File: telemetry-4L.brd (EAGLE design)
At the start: 69.8 x 22.9 mm, 69 parts, among them SW1 MF-SW-TACT-4.2MM, SW2 PCM12SMTR, U1 ATSAMD21G18A-MUT, U2 SPX3819M5-L-3-0, U3 MCP73831T-2ACI/OT, U4 IRLML6344TRPBF, U5 SIM868, U6 BMP280, U7 MPU-9250, U8 TPS61253YFFR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

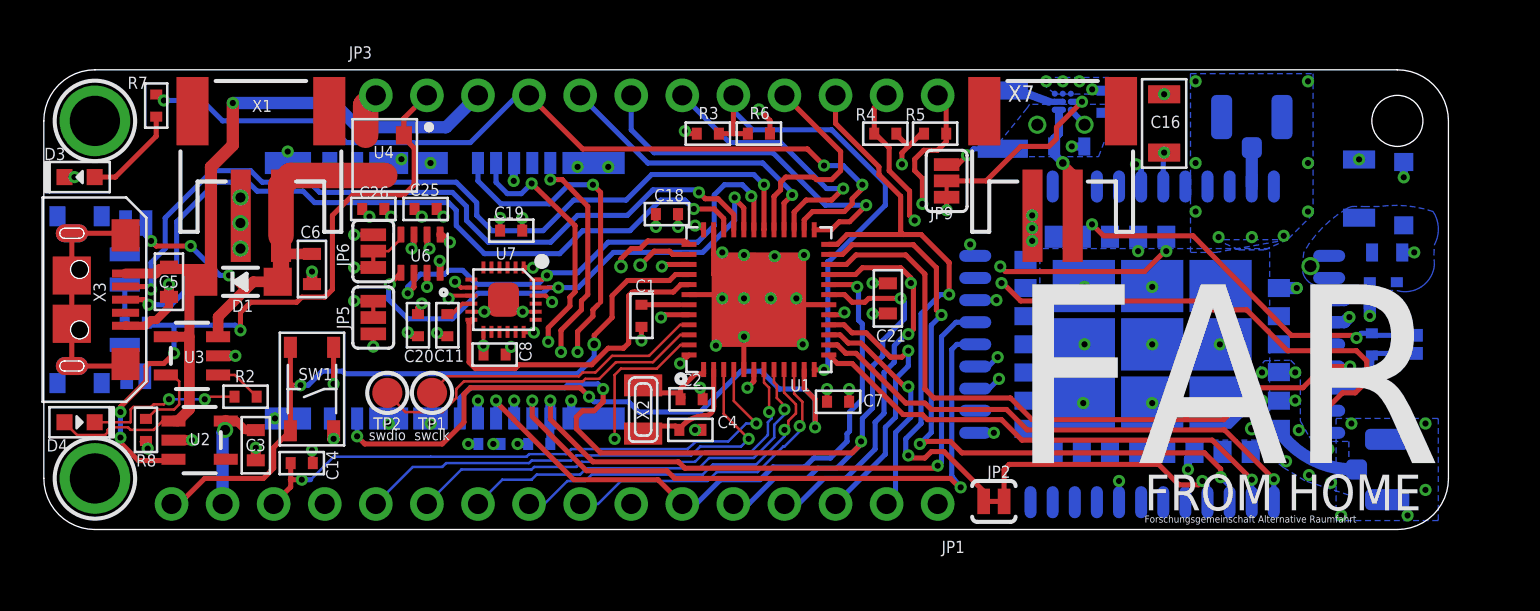
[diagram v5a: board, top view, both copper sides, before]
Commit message: Added MPR and POPULATE attributes - didnt seem to do anything though
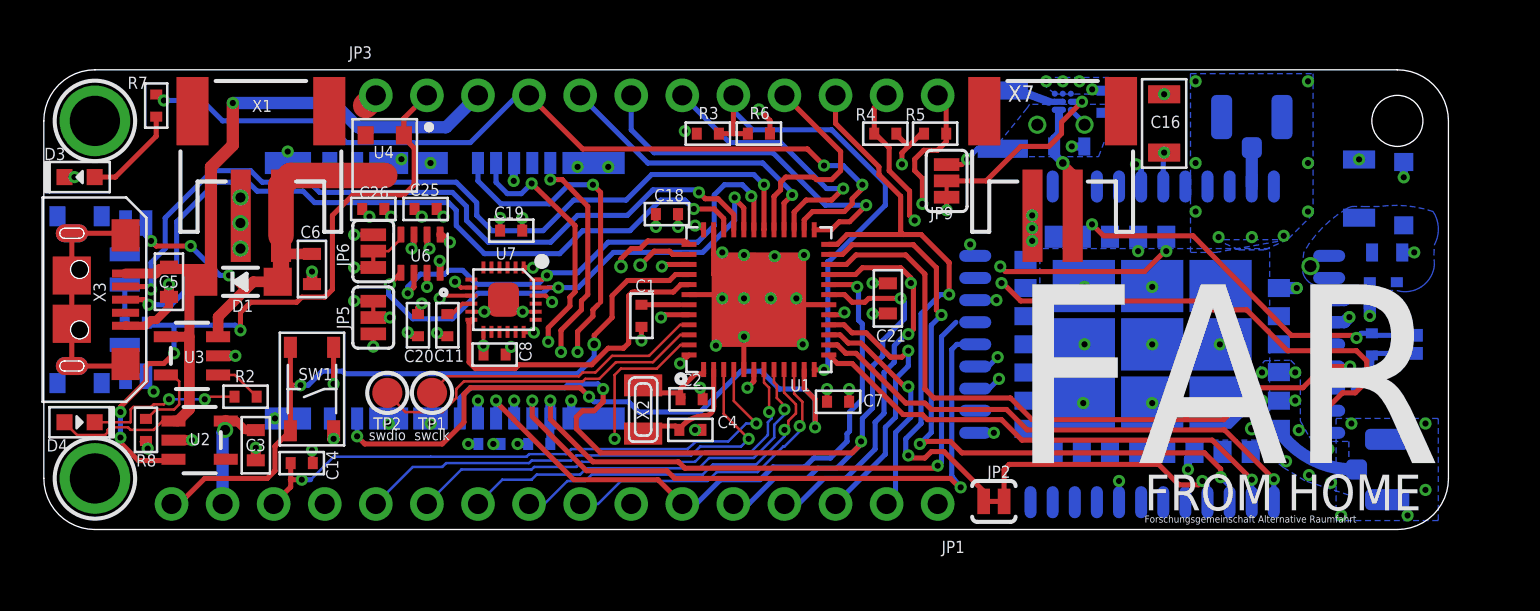
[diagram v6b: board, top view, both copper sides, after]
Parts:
- JP7: value JUMPER-PAD-2-NOYES_SILK -> JUMPER-PAD-2-NC_BY_TRACE; device SparkFun-Passives:PAD-JUMPER-2-NO_YES_SILK -> SparkFun-Passives:PAD-JUMPER-2-NC_BY_TRACE_YES_SILK
- L1: value 1277AS-H-1R0M=P2 -> 1uH
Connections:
- new net P$1: JP3.1
- net VBAT_ON: no longer JP3.1
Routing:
- net VBAT_ON: track 59.2 -> 53.1 mm
- net N$2: track 1.19 -> 5.59 mm, vias 1 -> 2
- net GND: track 70.4 -> 71.7 mm, vias 114 -> 115
- net VDD_EXT_2V8: track 5.17 -> 3.98 mm
- net SIM_VDD: track 31.9 -> 31.0 mm
- net P$1: track 0.00 -> 0.71 mm

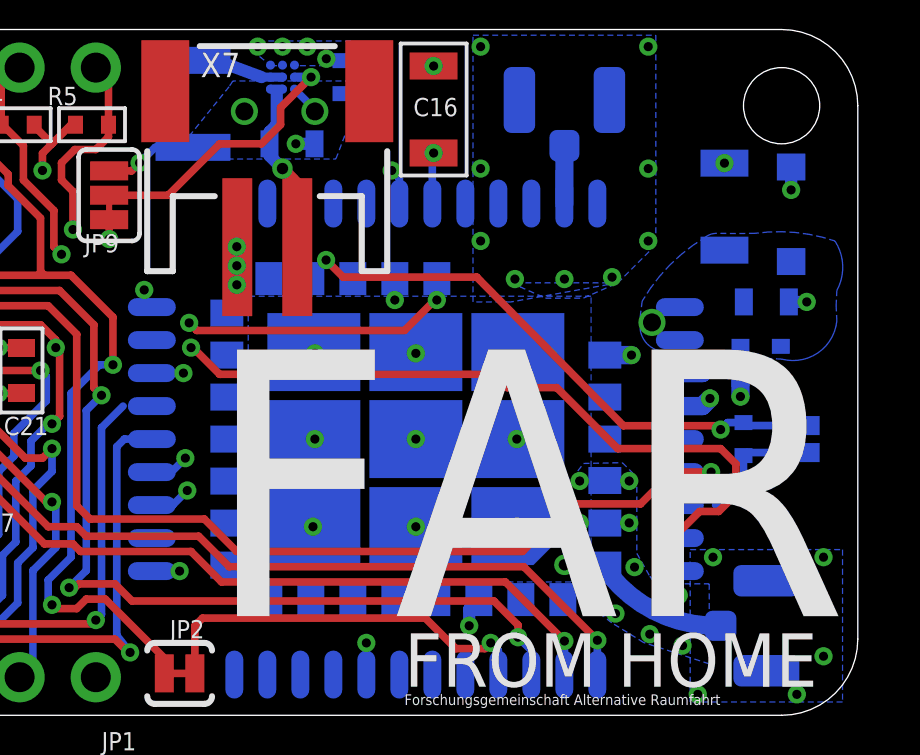
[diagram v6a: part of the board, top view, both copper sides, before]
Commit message: Added a 100uF cap to 5V output
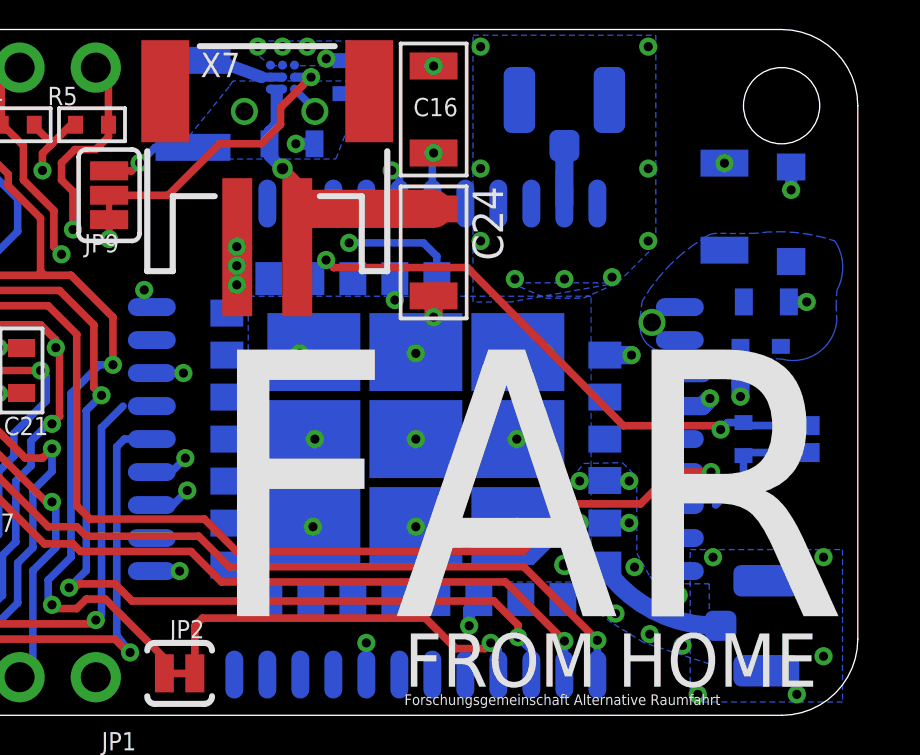
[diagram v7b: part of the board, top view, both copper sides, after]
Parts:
- added C24: 100uF, MF_Passives:C1206
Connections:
- net 5.0V: now also C24.P$1
- net GND: now also C24.P$2
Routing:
- net TX5/GPS_RX: track 34.9 -> 40.4 mm, vias 3 -> 2
- net 5.0V: track 6.26 -> 11.7 mm
- net STATUS: track 45.3 -> 41.7 mm, vias 3 -> 2
- net RX5/GPS_TX: track 31.2 -> 30.3 mm
- net GND: track 71.7 -> 72.4 mm, vias 115 -> 116

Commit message: tweaks
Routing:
- net TX5/GPS_RX: track 40.4 -> 39.9 mm
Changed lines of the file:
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@@
 <wire x1="40.1955" y1="13.462" x2="45.0215" y2="13.462" width="0.254" layer="15"/>
 <wire x1="45.0215" y1="13.462" x2="45.6565" y2="12.827" width="0.254" layer="15"/>
-<wire x1="54.483" y1="12.827" x2="45.6565" y2="12.827" width="0.254" layer="15"/>
-<wire x1="54.737" y1="14.605" x2="54.0385" y2="14.605" width="0.254" layer="15"/>
+<wire x1="54.229" y1="12.827" x2="45.6565" y2="12.827" width="0.254" layer="15"/>
+<wire x1="54.483" y1="14.605" x2="54.0385" y2="14.605" width="0.254" layer="15"/>
 <wire x1="54.0385" y1="14.605" x2="52.8955" y2="15.748" width="0.254" layer="15"/>
 <via x="52.8955" y="15.748" extent="1-16" drill="0.3048"/>
@@
 <wire x1="55.8165" y1="15.3035" x2="55.8165" y2="14.559" width="0.254" layer="16"/>
 <wire x1="55.8165" y1="14.559" x2="55.818" y2="14.5575" width="0.254" layer="16"/>
-<wire x1="54.483" y1="12.827" x2="55.1815" y2="13.5255" width="0.254" layer="15"/>
-<wire x1="55.1815" y1="13.5255" x2="55.1815" y2="14.1605" width="0.254" layer="15"/>
-<wire x1="55.1815" y1="14.1605" x2="54.737" y2="14.605" width="0.254" layer="15"/>
+<wire x1="54.229" y1="12.827" x2="54.9275" y2="13.5255" width="0.254" layer="15"/>
+<wire x1="54.9275" y1="13.5255" x2="54.9275" y2="14.1605" width="0.254" layer="15"/>
+<wire x1="54.9275" y1="14.1605" x2="54.483" y2="14.605" width="0.254" layer="15"/>
 </signal>
 <signal name="RX5/GPS_TX">
 <contactref element="U1" pad="38"/>
 <contactref element="U5" pad="61_"/>
-<wire x1="54.418" y1="14.5575" x2="54.418" y2="13.843" width="0.254" layer="16"/>
-<via x="54.418" y="13.843" extent="1-16" drill="0.3048"/>
+<wire x1="54.418" y1="14.5575" x2="54.164" y2="13.843" width="0.254" layer="16"/>
+<via x="54.164" y="13.843" extent="1-16" drill="0.3048"/>
 <wire x1="32.085" y1="13.68" x2="31.278" y2="13.68" width="0.254" layer="1"/>
 <wire x1="31.278" y1="13.68" x2="31.115" y2="13.843" width="0.254" layer="1"/>
@@
 <wire x1="45.974" y1="13.335" x2="46.6725" y2="13.335" width="0.254" layer="15"/>
 <wire x1="46.6725" y1="13.335" x2="47.0535" y2="13.716" width="0.254" layer="15"/>
-<wire x1="54.291" y1="13.97" x2="54.418" y2="13.843" width="0.254" layer="15"/>
-<wire x1="47.0535" y1="13.716" x2="54.2925" y2="13.716" width="0.254" layer="15"/>
-<wire x1="54.2925" y1="13.716" x2="54.4195" y2="13.843" width="0.254" layer="15"/>
-<wire x1="54.4195" y1="13.843" x2="54.418" y2="13.843" width="0.254" layer="15"/>
+<wire x1="53.021" y1="13.97" x2="54.164" y2="13.843" width="0" layer="19" extent="1-16"/>
+<wire x1="47.0535" y1="13.716" x2="54.0385" y2="13.716" width="0.254" layer="15"/>
+<wire x1="54.0385" y1="13.716" x2="54.1655" y2="13.843" width="0.254" layer="15"/>
+<wire x1="54.1655" y1="13.843" x2="54.164" y2="13.843" width="0.254" layer="15"/>
 </signal>
 <signal name="GPS_EN_">
@@
 <contactref element="SW2" pad="O"/>
 <contactref element="JP7" pad="2"/>
-<wire x1="4.028" y1="9.18" x2="4.122" y2="9.086" width="0.254" layer="16"/>
-<wire x1="4.122" y1="9.086" x2="4.064" y2="7.62" width="0.254" layer="16"/>
+<wire x1="4.028" y1="9.18" x2="4.0585" y2="9.1495" width="0.254" layer="16"/>
+<wire x1="4.0585" y1="9.1495" x2="4.064" y2="7.62" width="0.254" layer="16"/>
 </signal>
 <signal name="N$13">
